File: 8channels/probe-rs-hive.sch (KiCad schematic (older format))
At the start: 16 parts, among them J1 Conn_01x18_Female, J2 Conn_01x18_Male, P1 PCIEX1_02X18, P2 PCIEX1_02X18, U1 SN74CB3Q3251PWR, U2 SN74CB3Q3251PWR, U3 SN74CB3Q3251PWR, U4 SN74CB3Q3251PWR

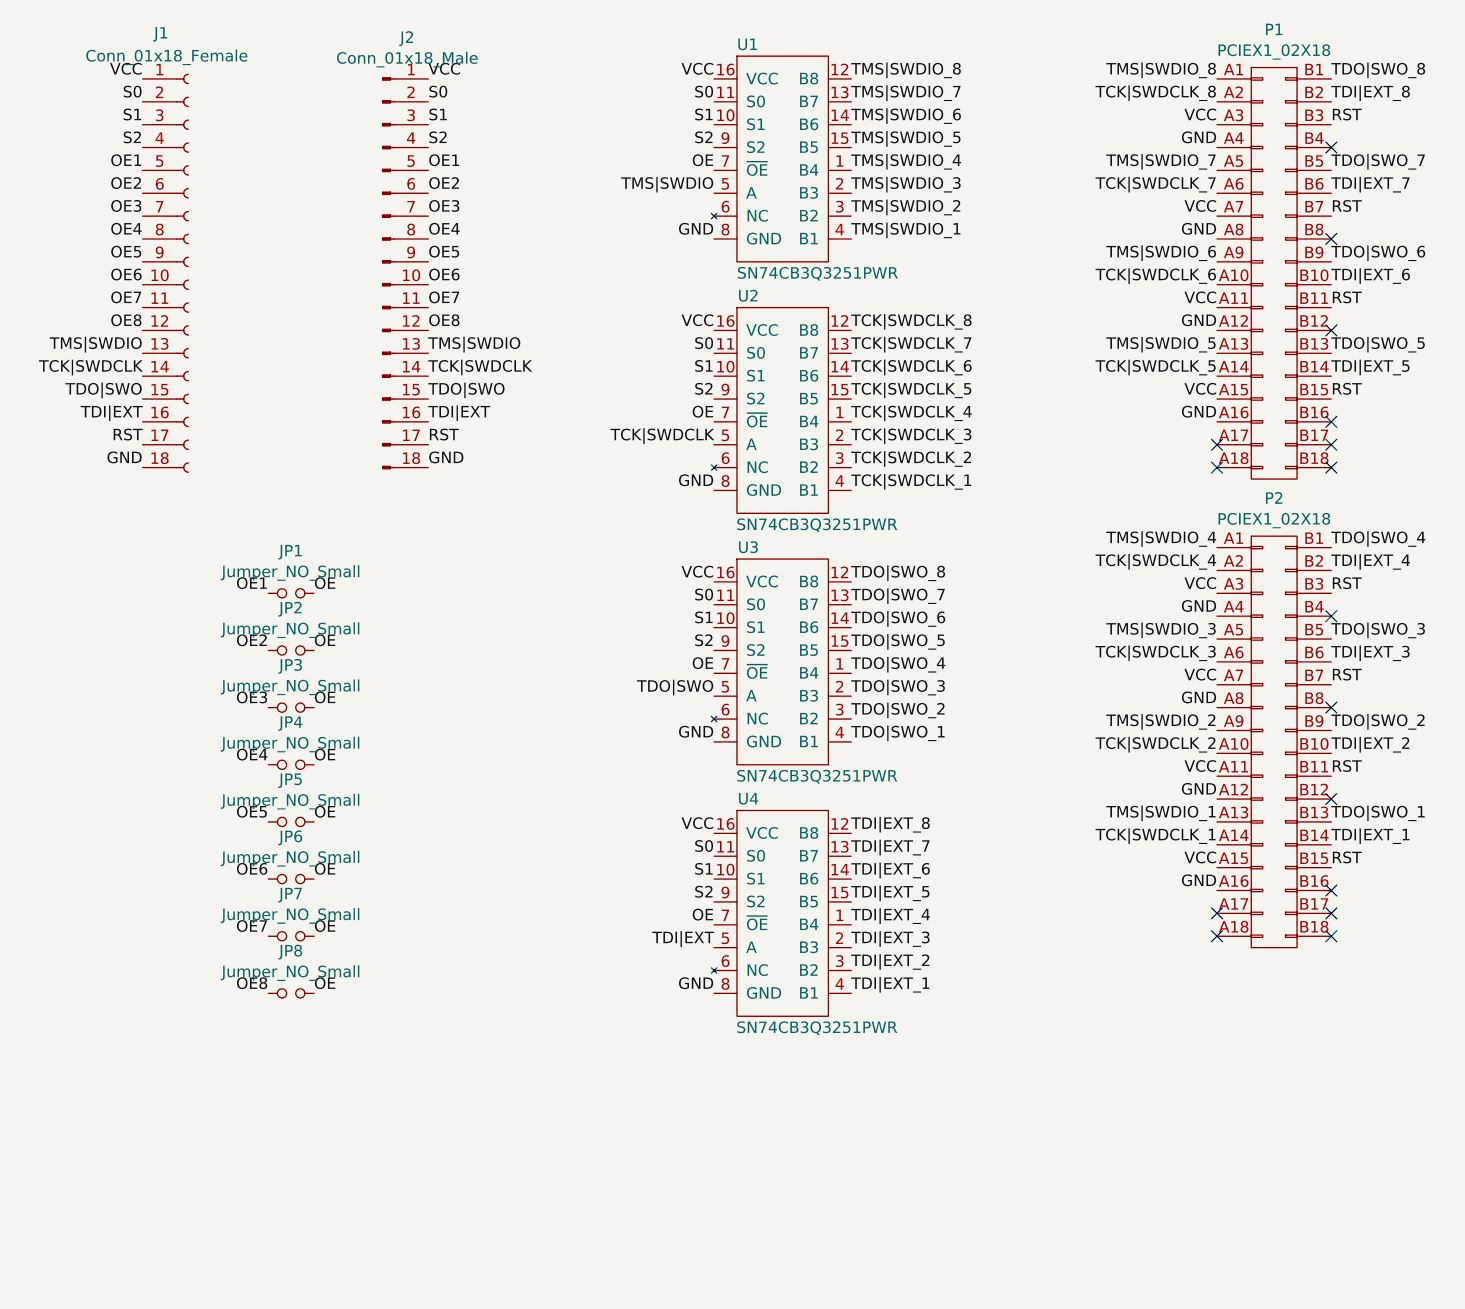
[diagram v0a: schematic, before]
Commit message: Add a line buffer/multiplexer to RST
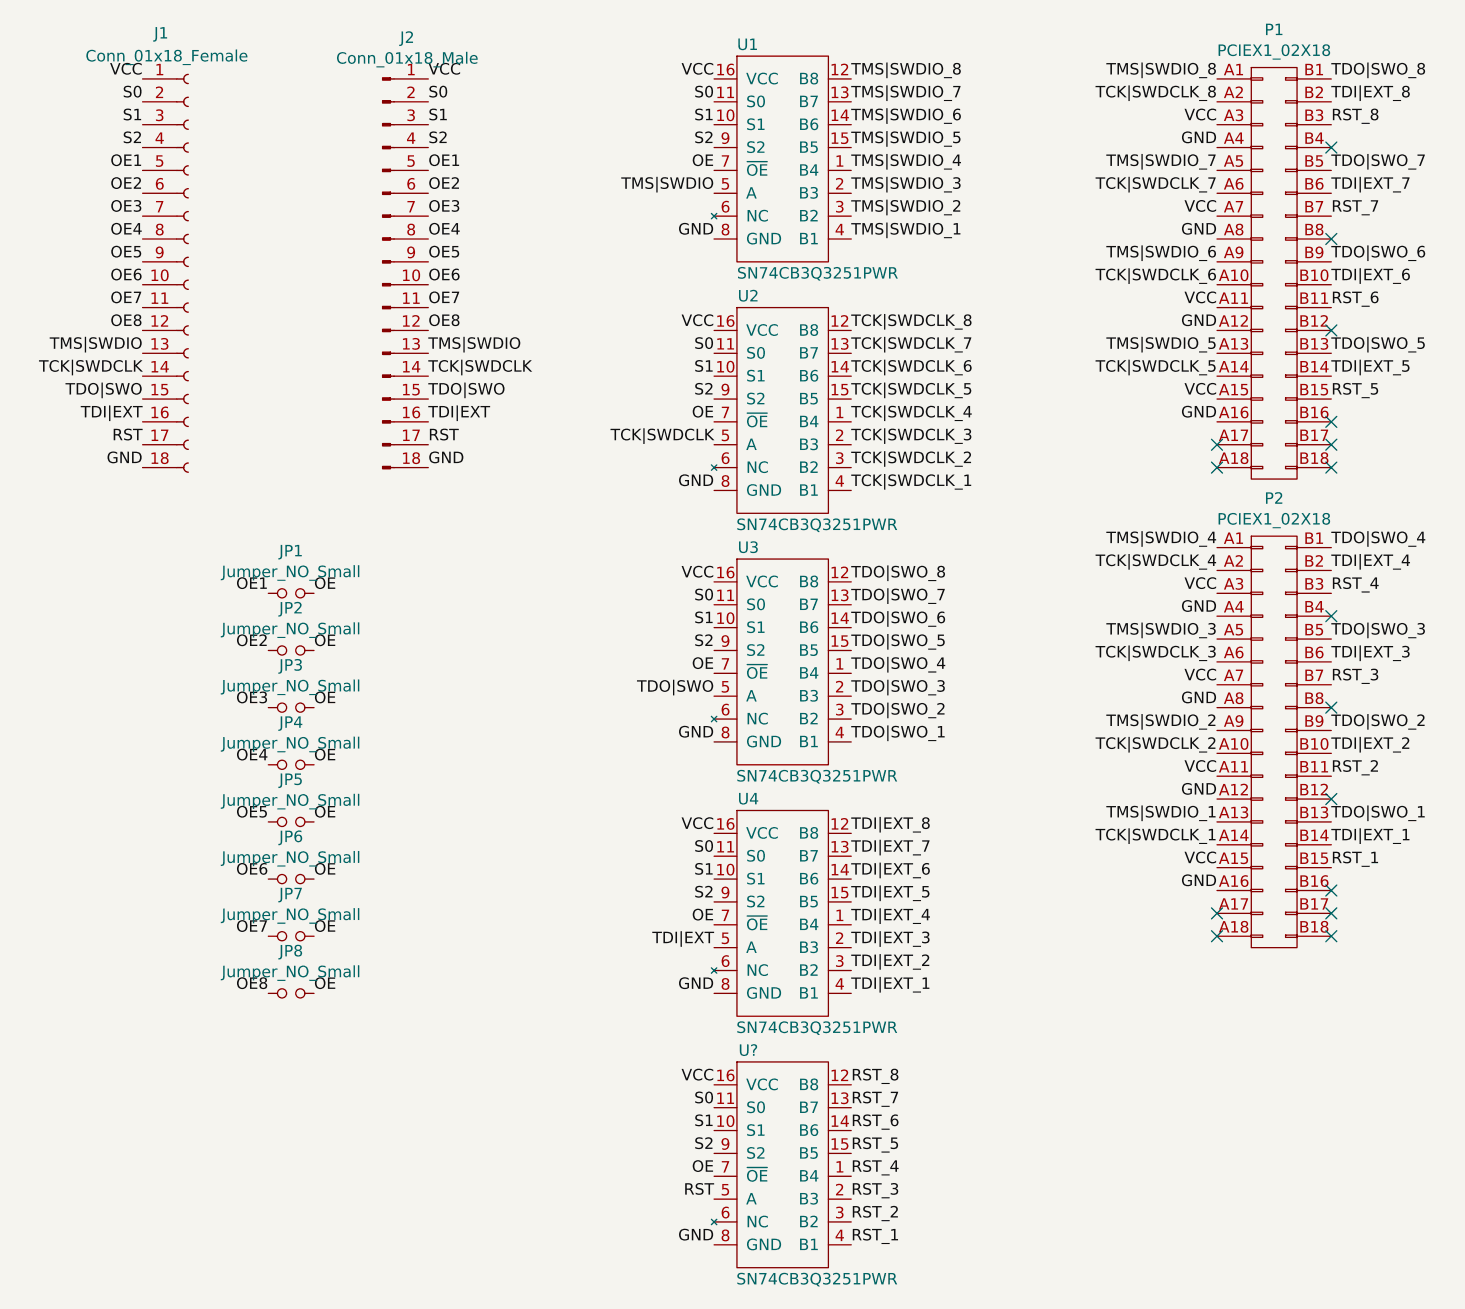
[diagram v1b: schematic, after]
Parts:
- added U?: SN74CB3Q3251PWR, probe-rs-hive:R-PVQFN-N16, symbol probe-rs-hive:SN74CB3Q3251PWR
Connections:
- net GND: now also U?.8 (GND)
- net OE: now also U?.7 (~OE)
- net RST: now also U?.5 (A); no longer P1.B11 (P22), P1.B15 (P30), P1.B3 (P6), P1.B7 (P14), P2.B11 (P22), P2.B15 (P30), P2.B3 (P6), P2.B7 (P14)
- net S0: now also U?.11 (S0)
- net S1: now also U?.10 (S1)
- net S2: now also U?.9 (S2)
- net VCC: now also U?.16 (VCC)
- new net RST_1: P2.B15 (P30), U?.4 (B1)
- new net RST_2: P2.B11 (P22), U?.3 (B2)
- new net RST_3: P2.B7 (P14), U?.2 (B3)
- new net RST_4: P2.B3 (P6), U?.1 (B4)
- new net RST_5: P1.B15 (P30), U?.15 (B5)
- new net RST_6: P1.B11 (P22), U?.14 (B6)
- new net RST_7: P1.B7 (P14), U?.13 (B7)
- new net RST_8: P1.B3 (P6), U?.12 (B8)
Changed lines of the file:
@@
 EESchema Schematic File Version 4
-LIBS:probe-rs-hive-cache
 EELAYER 30 0
 EELAYER END
@@
 TDI|EXT
 Text Label 6250 1050 0    50   ~ 0
-RST
+RST_8
 Text Label 6250 1450 0    50   ~ 0
-RST
+RST_7
 Text Label 6250 1850 0    50   ~ 0
-RST
+RST_6
 Text Label 6250 2250 0    50   ~ 0
-RST
+RST_5
 Text Label 6250 3100 0    50   ~ 0
-RST
+RST_4
 Text Label 6250 3500 0    50   ~ 0
-RST
+RST_3
 Text Label 6250 3900 0    50   ~ 0
-RST
+RST_2
 Text Label 6250 4300 0    50   ~ 0
-RST
+RST_1
 NoConn ~ 6250 1150
 NoConn ~ 6250 1550
@@
 NoConn ~ 5750 4500
 NoConn ~ 5750 4600
+Text Label 4150 5250 0    50   ~ 0
+RST_8
+Text Label 4150 5350 0    50   ~ 0
+RST_7
+Text Label 4150 5450 0    50   ~ 0
+RST_6
+Text Label 4150 5550 0    50   ~ 0
+RST_5
+Text Label 4150 5650 0    50   ~ 0
+RST_4
+Text Label 4150 5750 0    50   ~ 0
+RST_3
+Text Label 4150 5850 0    50   ~ 0
+RST_2
+Text Label 4150 5950 0    50   ~ 0
+RST_1
+$Comp
+L probe-rs-hive:SN74CB3Q3251PWR U?
+U 1 1 5FB06162
+P 3850 5600
+AR Path="/5E6BE00C/5FB06162" Ref="U?"  Part="1"
+AR Path="/5E768EC7/5FB06162" Ref="U?"  Part="1"
+AR Path="/5E769194/5FB06162" Ref="U?"  Part="1"
+AR Path="/5E769690/5FB06162" Ref="U?"  Part="1"
+AR Path="/5FB06162" Ref="U?"  Part="1"
+F 0 "U?" H 3700 6100 50  0000 C CNN
+F 1 "SN74CB3Q3251PWR" H 4000 5100 50  0000 C CNN
+F 2 "probe-rs-hive:R-PVQFN-N16" H 3850 5000 50  0001 C CNN
+F 3 "" H 3550 5250 50  0001 C CNN
+	1    3850 5600
+	1    0    0    -1
+$EndComp
+Text Label 3550 5250 2    50   ~ 0
+VCC
+Text Label 3550 5950 2    50   ~ 0
+GND
+Text Label 3550 5350 2    50   ~ 0
+S0
+Text Label 3550 5450 2    50   ~ 0
+S1
+Text Label 3550 5550 2    50   ~ 0
+S2
+Text Label 3550 5650 2    50   ~ 0
+OE
+Text Label 3550 5750 2    50   ~ 0
+RST
 $EndSCHEMATC
